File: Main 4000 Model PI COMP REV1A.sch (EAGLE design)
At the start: 119 parts, among them IC1 QUAD_OPAMPD, IC2 7818TV, IC3 TL331, IC4 TUSB2036, Q1 16MHZ, Q2 TIP120, Q3 BC846, Q4 BC846, U1 RFM69HCW, U3 MAX98306ETD+, U4 ADS1015

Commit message: Routed Pi version
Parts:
- added TP1: PTR1PAD1-13, testpad:PTR1PAD1-13
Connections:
- net N$149: now also TP1.TP
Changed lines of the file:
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@@
 <part name="GND2" library="SparkFun-Aesthetics" deviceset="GND" device=""/>
 <part name="JP5" library="pinhead" deviceset="PINHD-1X2" device=""/>
+<part name="TP1" library="testpad" deviceset="PTR1" device="PAD1-13"/>
 </parts>
 <sheets>
@@
 <instance part="JP4" gate="G$1" x="50.8" y="83.82"/>
 <instance part="GND2" gate="1" x="33.02" y="48.26"/>
+<instance part="TP1" gate="G$1" x="99.06" y="86.36"/>
 </instances>
 <busses>
@@
 <wire x1="99.06" y1="88.9" x2="99.06" y2="93.98" width="0.1524" layer="91"/>
 <pinref part="JP4" gate="G$1" pin="GP22"/>
-</segment>
-</net>
+<pinref part="TP1" gate="G$1" pin="TP"/>
+<junction x="99.06" y="88.9"/>
+</segment>
+</net>

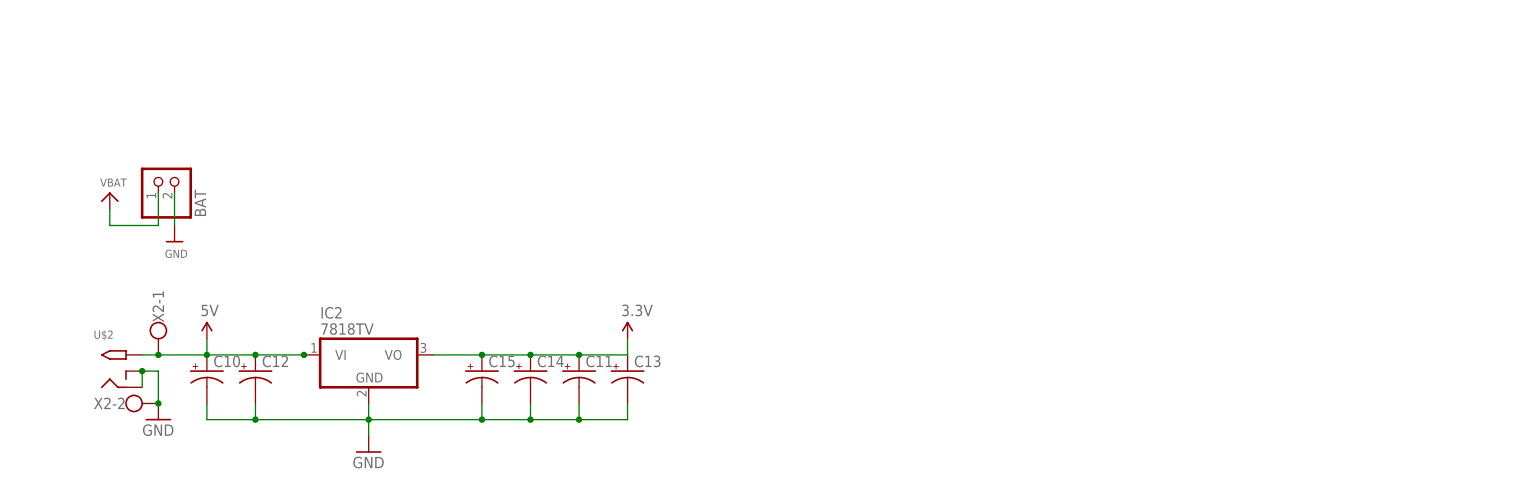
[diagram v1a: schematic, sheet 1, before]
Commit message: Added boost circuit
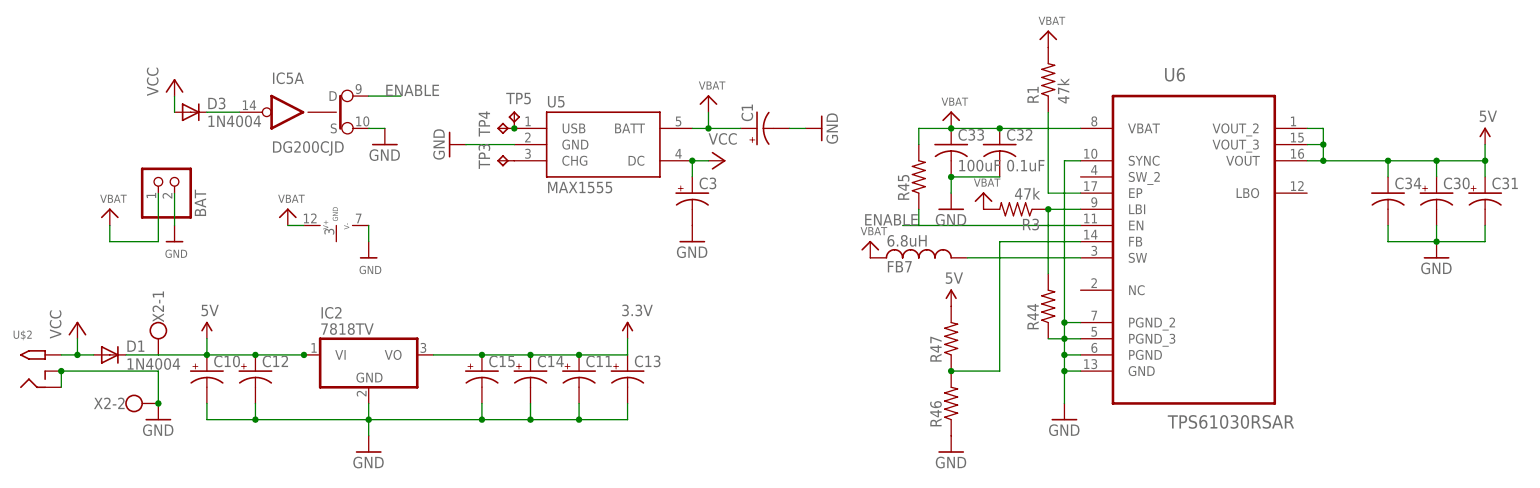
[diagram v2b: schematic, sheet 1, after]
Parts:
- added C1, C3, C30, C31: (no value), rcl:CPOL-USE1.8-4
- added C32: 0.1uF, rcl:C-USC0805
- added C33: 100uF, rcl:C-USC0805
- added C34: (no value), rcl:C-USC0805
- added D1, D3: 1N4004, adafruit:1N4004
- added FB7: 6.8uH, ELL-i-Passives:FB-0805-A
- added IC5: DG200CJD, linear:DG200CJD
- added R1, R3: 47k, rcl:R-US_R0805
- added R44, R45, R46, R47: (no value), rcl:R-US_R0805
- added TP3, TP4, TP5: TPTP20SQ, testpad:TPTP20SQ
- added U5: MAX1555, SparkFun-PowerIC:MAX1555
- added U6: TPS61030RSAR, Texas Instruments_By_element14_Batch_1:TPS61030RSAR
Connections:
- new net ENABLE: IC5A.D, R45.1, U6.EN
- new net FB: R46.2, R47.1, U6.FB
- new net N$193: D3.C, IC5A.IN
- new net N$196: FB7.2, U6.SW
- new net N$197: R1.1, U6.EP
- new net N$198: R3.1, R44.2, U6.LBI
- new net N$95: TP3.TP, U5.CHG
- new net N$96: TP4.TP, TP5.TP, U5.USB
- new net VCC: C3.+, D1.A, D3.A, U$2.TIP, U5.DC
- net 5V: now also C30.+, C31.+, C34.1, D1.C, R47.2, U6.VOUT, U6.VOUT_2, U6.VOUT_3; no longer U$2.TIP
- net GND: now also C1.-, C3.-, C30.-, C31.-, C32.2, C33.2, C34.2, IC5A.S, IC5P.V-, R44.1, R46.1, U5.GND, U6.GND, U6.PGND, U6.PGND_2, U6.PGND_3, U6.SYNC
- net VBAT: now also C1.+, C32.1, C33.1, FB7.1, IC5P.V+, R1.2, R3.2, R45.2, U5.BATT, U6.VBAT
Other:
- moved on the sheet: U$2
